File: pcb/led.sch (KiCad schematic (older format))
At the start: 10 parts, among them J1 CONN_01X03, J2 CONN_01X03, J3 CONN_01X04, U1 DSN-MINI-360, U2 4504, U3 4504

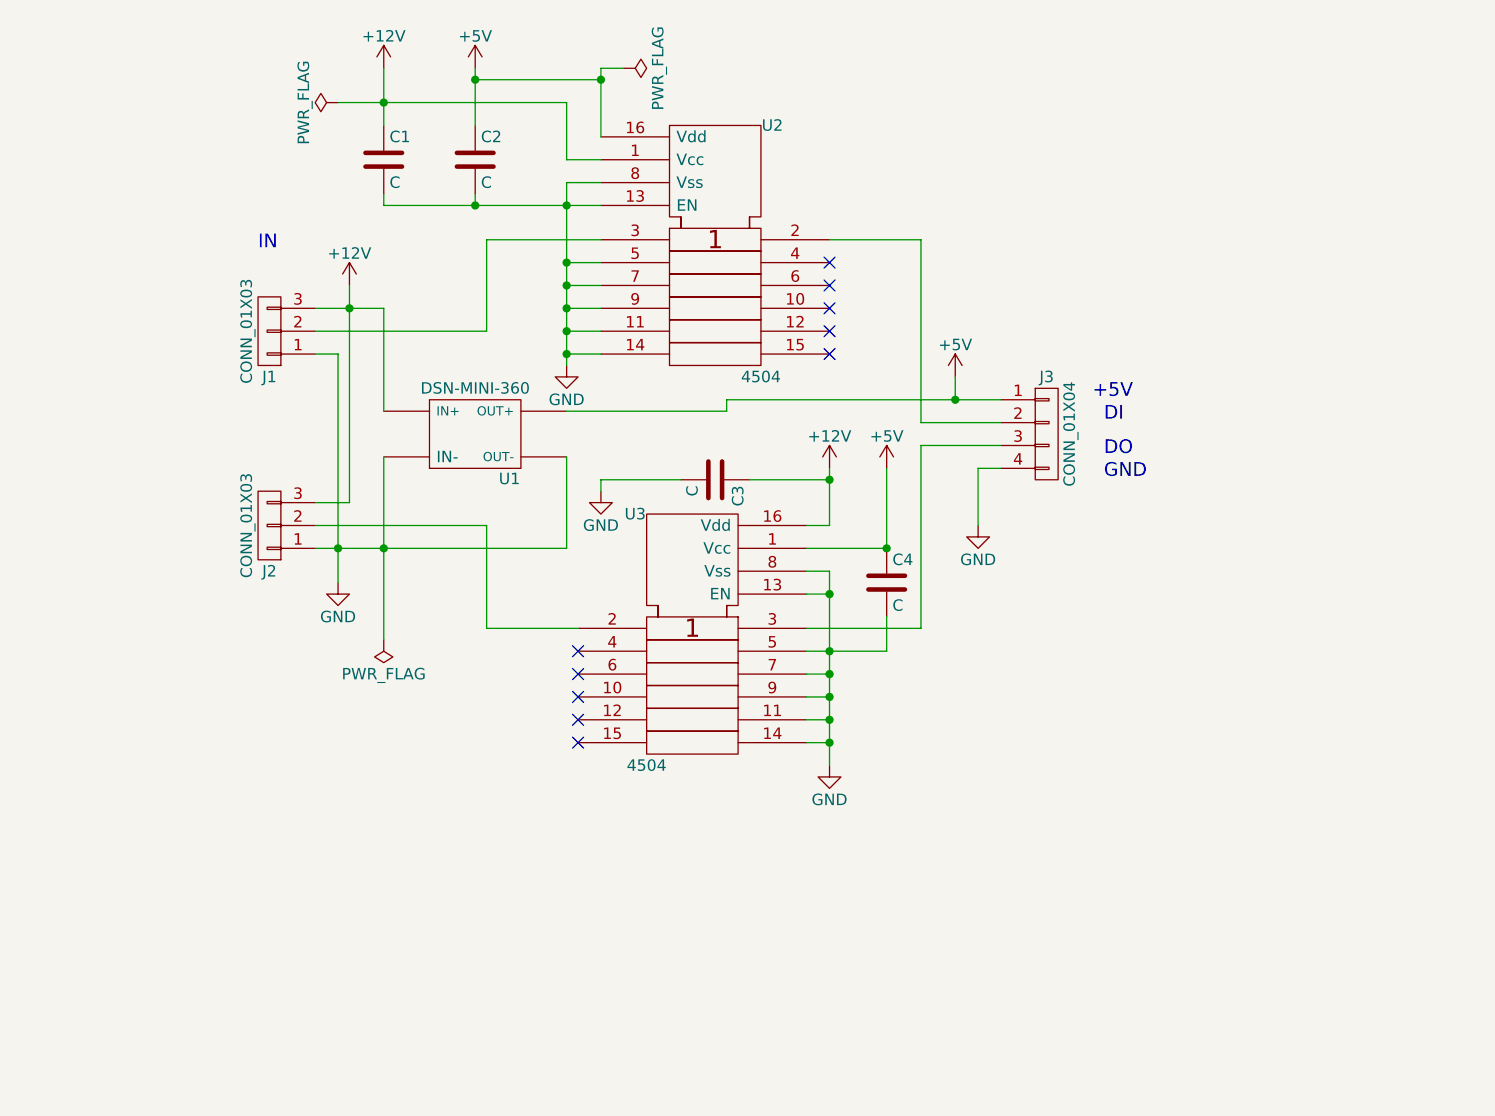
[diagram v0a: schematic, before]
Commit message: Adapt for optional 1-wire operation.
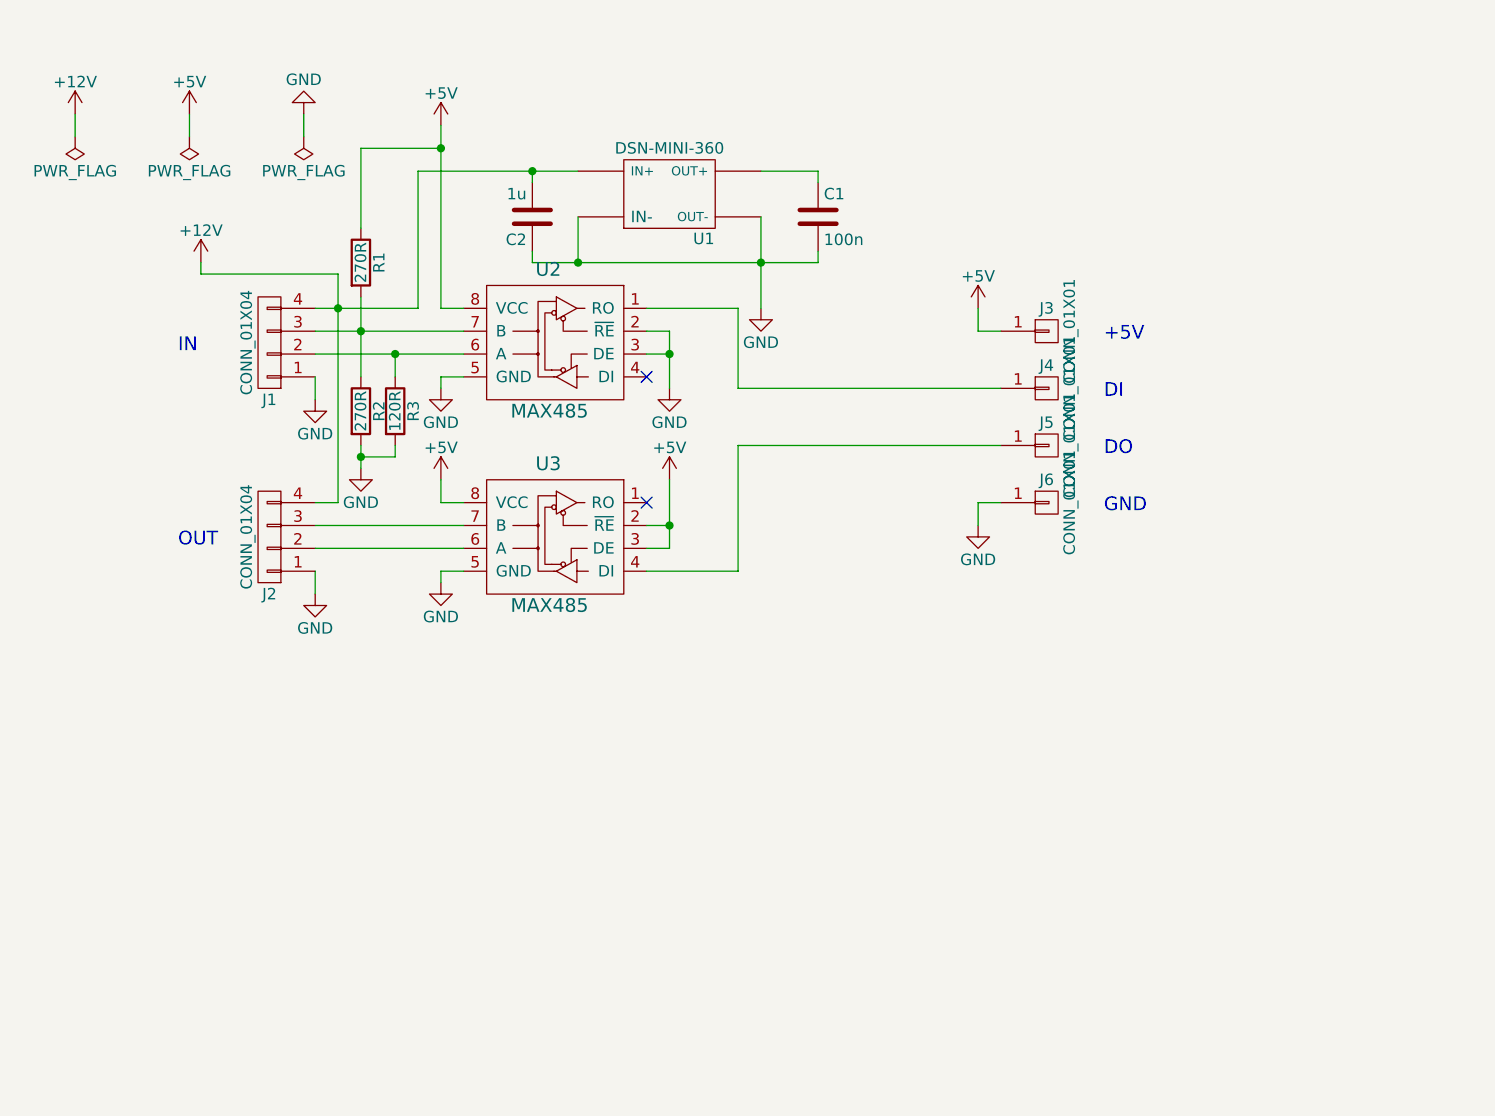
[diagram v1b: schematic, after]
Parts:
- removed C3, C4: C, Capacitors_SMD:C_0603, symbol C
- removed J1, J2: CONN_01X03, Connectors_Phoenix:PhoenixContact_MSTBA-G_03x5.08mm_Angled, symbol CONN_01X03
- removed J3: CONN_01X04, Pin_Headers:Pin_Header_Straight_1x04_Pitch2.54mm, symbol CONN_01X04
- removed U2, U3: 4504, Housings_SOIC:SOIC-16_3.9x9.9mm_Pitch1.27mm, symbol 4504
- added J1, J2: CONN_01X04, Connectors_Phoenix:PhoenixContact_MSTBA-G_04x5.08mm_Angled, symbol CONN_01X04
- added J3, J4, J5, J6: CONN_01X01, Wire_Pads:SolderWirePad_single_1-5mmDrill, symbol CONN_01X01
- added R1: 270R, symbol R
- added R2: 270R, Resistors_SMD:R_0603, symbol R
- added R3: 120R, Resistors_SMD:R_0603, symbol R
- added U2, U3: MAX485, Housings_SOIC:SOIC-8_3.9x4.9mm_Pitch1.27mm, symbol MAX485
- C1: value C -> 100n
- C2: value C -> 1u; footprint Capacitors_SMD:C_0603 -> Resistors_SMD:R_0805
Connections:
- net +12V: now also C2.2, J1.4 (P4), J2.4 (P4); no longer C1.1
- net +5V: now also J3.1 (P1), R1.1, U2.8 (VCC), U3.2 (~RE), U3.3 (DE), U3.8 (VCC); no longer C2.1, U1.OUT+
- net GND: now also C2.1, J1.1 (P1), J2.1 (P1), J6.1 (P1), R2.2, R3.2, U2.2 (~RE), U2.3 (DE), U2.5 (GND), U3.5 (GND); no longer C2.2
- new net: C1.1, U1.OUT+
- new net: J1.2 (P2), R3.1, U2.6 (A)
- new net: J1.3 (P3), R1.2, R2.1, U2.7 (B)
- new net: J2.2 (P2), U3.6 (A)
- new net: J2.3 (P3), U3.7 (B)
- new net: J4.1 (P1), U2.1 (RO)
- new net: J5.1 (P1), U3.4 (DI)
- no-connect marks 10 -> 2
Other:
- note added: "OUT"
- moved on the sheet: C1, C2, U1

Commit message: Use local libraries.
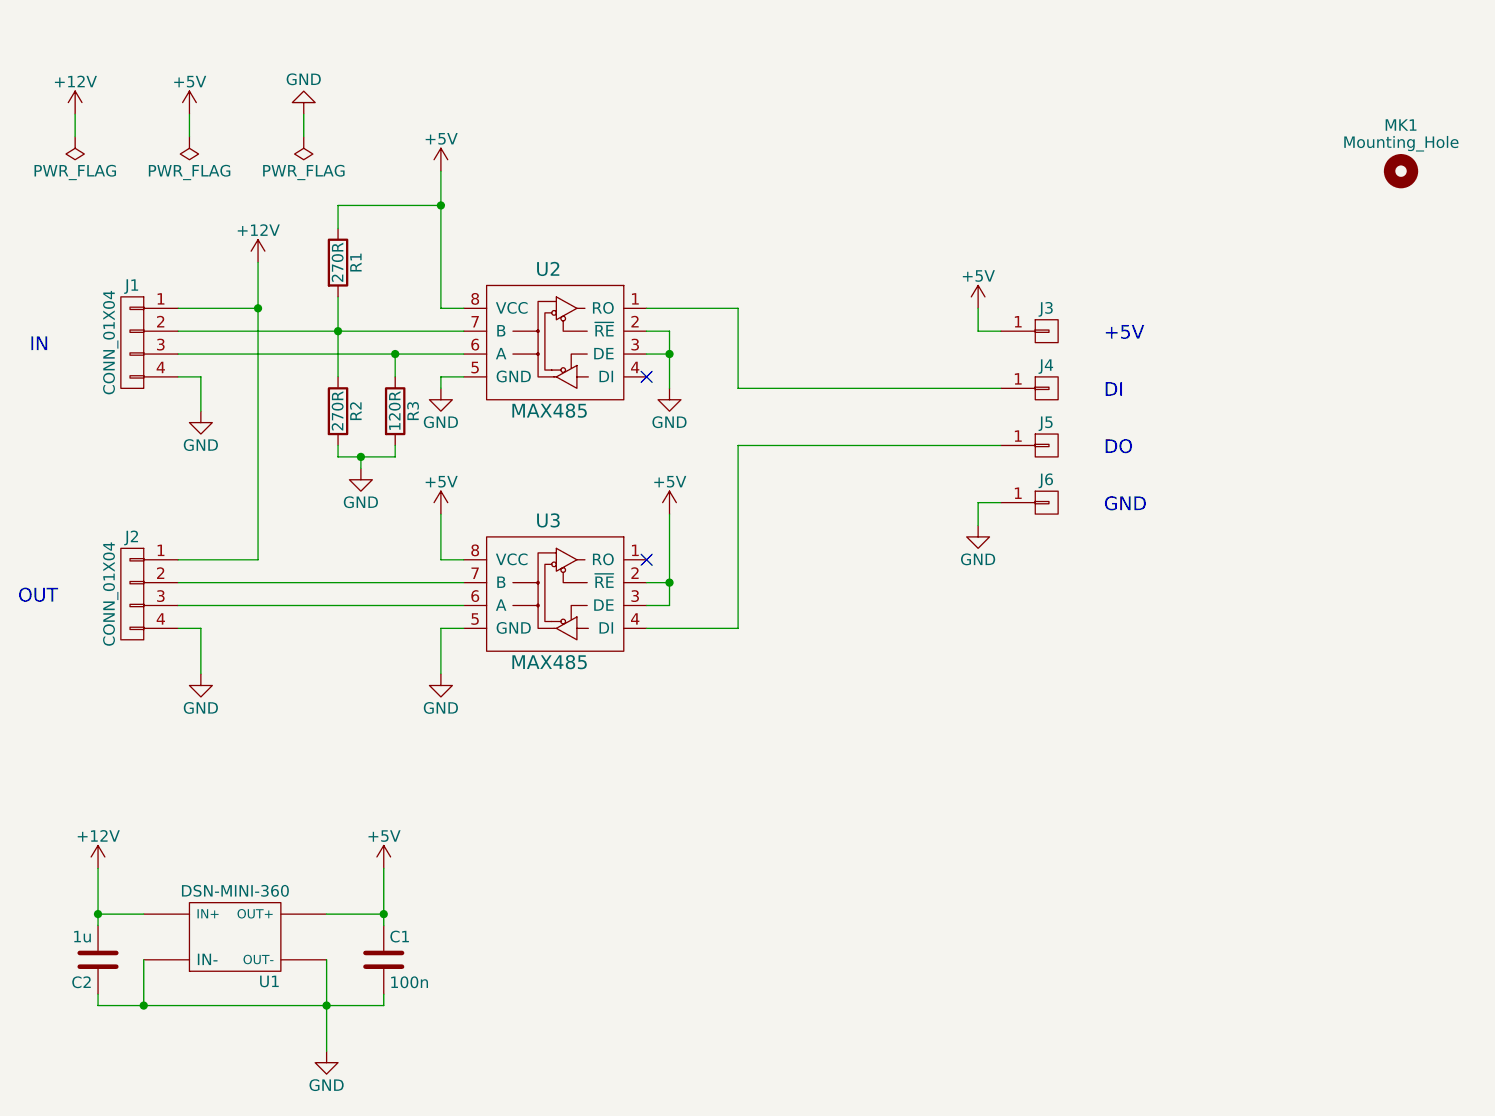
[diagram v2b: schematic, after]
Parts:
- added MK1: Mounting_Hole, symbol Mounting_Hole
- C2: footprint Resistors_SMD:R_0805 -> Capacitors_SMD:C_0805
- R1: footprint (none) -> Resistors_SMD:R_0603
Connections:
- net +12V: now also J1.1 (P1), J2.1 (P1); no longer J1.4 (P4), J2.4 (P4)
- net +5V: now also C1.1, U1.OUT+
- net GND: now also J1.4 (P4), J2.4 (P4); no longer J1.1 (P1), J2.1 (P1)
- net at R3.1, U2.6 (A): now also J1.3 (P3); no longer J1.2 (P2)
- net at R1.2, R2.1, U2.7 (B): now also J1.2 (P2); no longer J1.3 (P3)
- net at J2.2 (P2): now also U3.7 (B); no longer U3.6 (A)
- net at J2.3 (P3): now also U3.6 (A); no longer U3.7 (B)
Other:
- moved on the sheet: C1, C2, J1, J2, R1, R2, U1, U3

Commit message: Fix errors.
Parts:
- MK1: footprint (none) -> Mounting_Holes:MountingHole_3.5mm
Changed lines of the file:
@@
-$EndComp
-$Comp
-L DSN-MINI-360 U1
-U 1 1 58CEF9DF
-P 1700 4500
-F 0 "U1" H 1850 4304 50  0000 C CNN
-F 1 "DSN-MINI-360" H 1700 4700 50  0000 C CNN
-F 2 "dsn-mini-360:DSN-MINI-360" H 1700 4500 50  0001 C CNN
-F 3 "" H 1700 4500 50  0001 C CNN
-	1    1700 4500
-	1    0    0    -1
 $EndComp
 $Comp
@@
 F 0 "MK1" H 6800 1350 50  0000 C CNN
 F 1 "Mounting_Hole" H 6800 1275 50  0000 C CNN
-F 2 "" H 6800 1150 50  0001 C CNN
+F 2 "Mounting_Holes:MountingHole_3.5mm" H 6800 1150 50  0001 C CNN
 F 3 "" H 6800 1150 50  0001 C CNN
 	1    6800 1150
@@
 Wire Wire Line
 	2150 2350 2150 2400
+$Comp
+L DSN-MINI-360 U1
+U 1 1 58E10987
+P 1700 4500
+F 0 "U1" H 1850 4304 50  0000 C CNN
+F 1 "DSN-MINI-360" H 1700 4700 50  0000 C CNN
+F 2 "dsn-mini-360:DSN-MINI-360" H 1700 4500 50  0001 C CNN
+F 3 "" H 1700 4500 50  0001 C CNN
+	1    1700 4500
+	1    0    0    -1
+$EndComp
 $EndSCHEMATC
